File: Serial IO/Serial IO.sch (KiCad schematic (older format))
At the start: 28 parts, among them J1 Apple ][ Peripheral Adapter, J2 BaseboardConnector, J3 SPI Breakout, SW1 Reset Serial, U1 74AHCT04, U2 WD65C21, U3 74LS138, U4 MCP23S17_SP

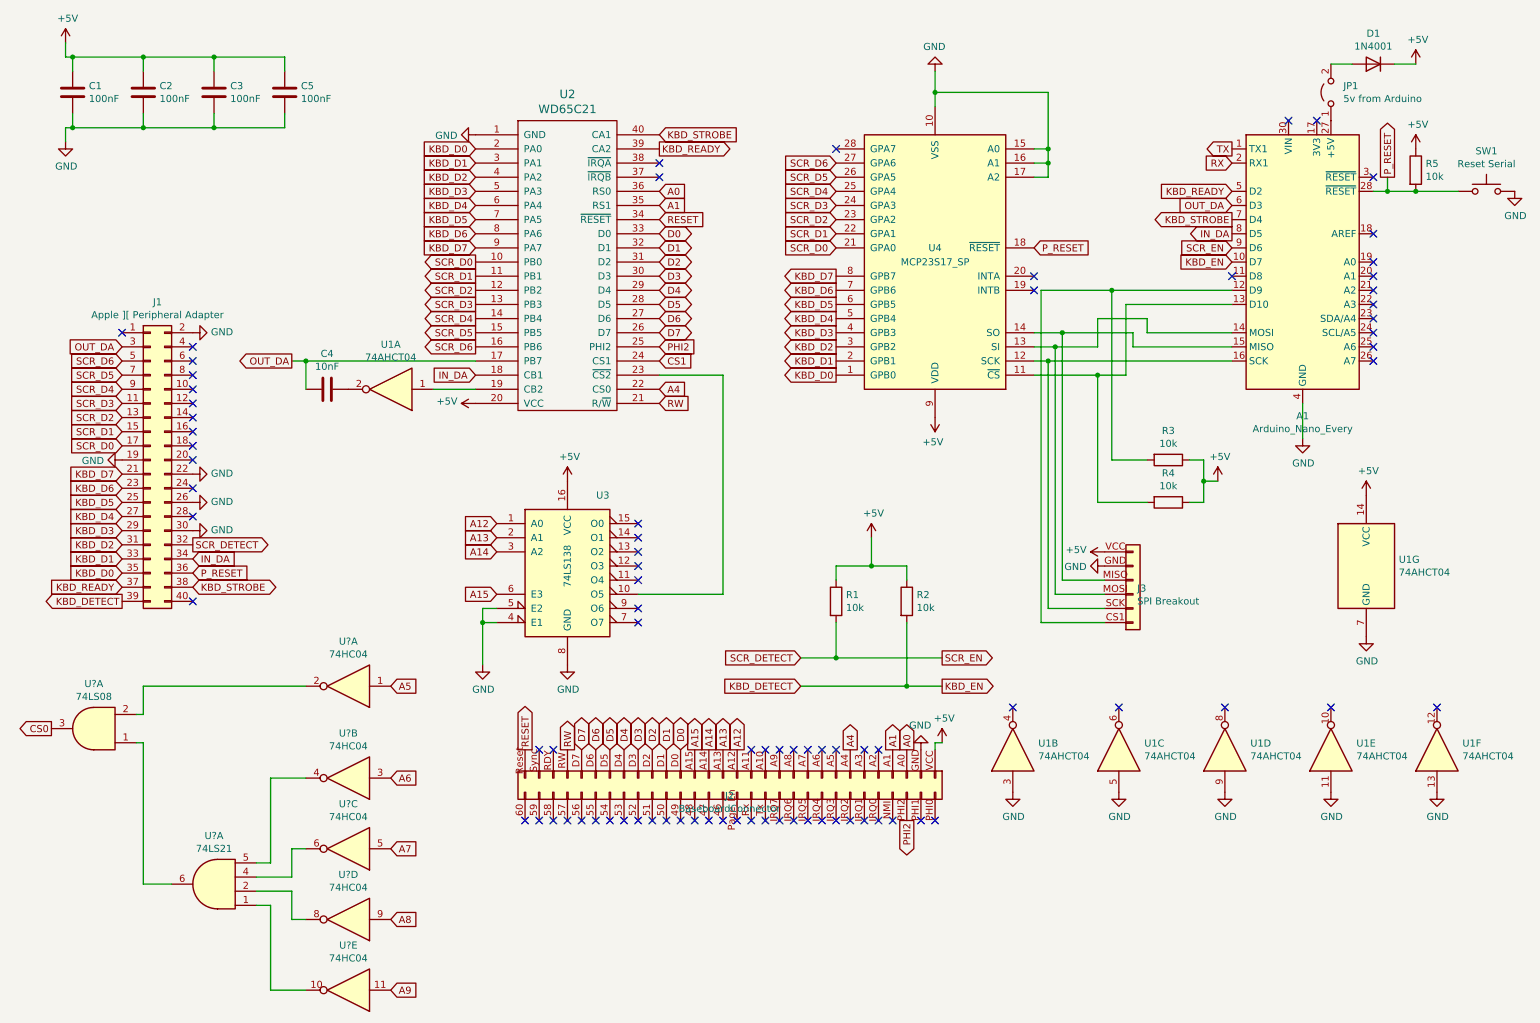
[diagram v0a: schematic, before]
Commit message: Updated Serial IO to use the 6522 VIA instead of the 6521 PIA
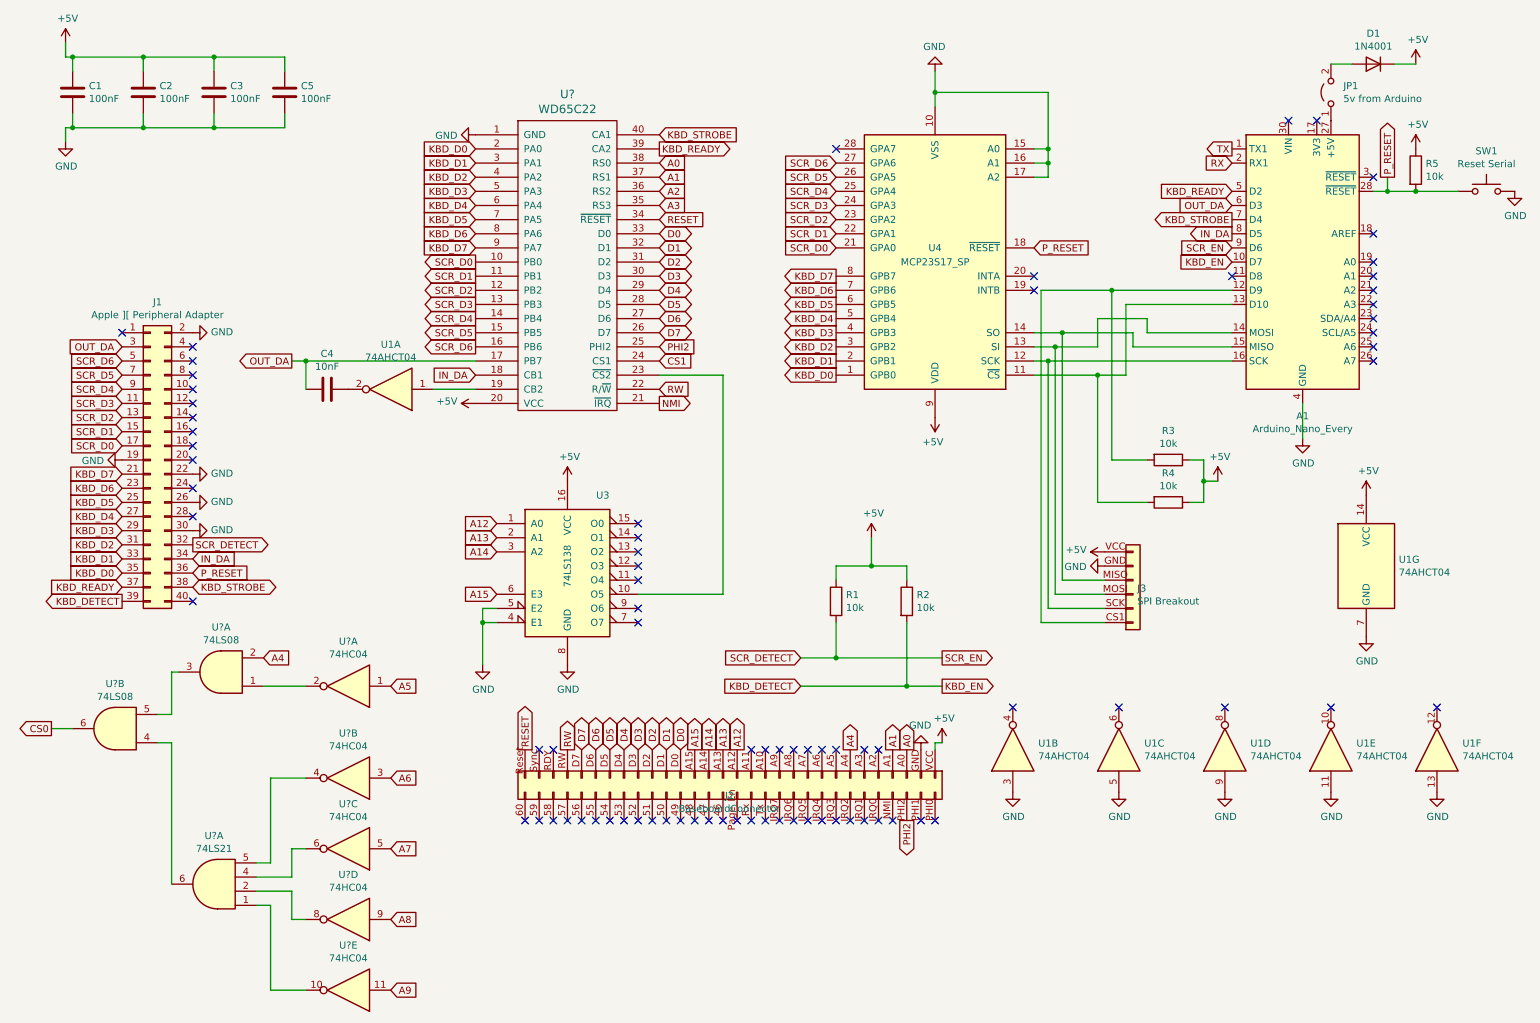
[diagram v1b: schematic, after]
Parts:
- removed U2: WD65C21, Package_DIP:DIP-40_W15.24mm_Socket_LongPads, symbol 65xx:WD65C21
- added U?: WD65C22, symbol 65xx:WD65C22
- added U?: 74LS08, symbol 74xx:74LS08
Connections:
- net +5V: now also U?.20 (VCC)
- net A0: now also U?.38 (RS0)
- net A1: now also U?.37 (RS1)
- net A4: now also U?.2
- net CS0: now also U?.6; no longer U?.3
- net CS1: now also U?.24 (CS1)
- net D0: now also U?.33 (D0)
- net D1: now also U?.32 (D1)
- net D2: now also U?.31 (D2)
- net D3: now also U?.30 (D3)
- net D4: now also U?.29 (D4)
- net D5: now also U?.28 (D5)
- net D6: now also U?.27 (D6)
- net D7: now also U?.26 (D7)
- net GND: now also U?.1 (GND)
- net IN_DA: now also U?.18 (CB1)
- net KBD_D0: now also U?.2 (PA0)
- net KBD_D1: now also U?.3 (PA1)
- net KBD_D2: now also U?.4 (PA2)
- net KBD_D3: now also U?.5 (PA3)
- net KBD_D4: now also U?.6 (PA4)
- net KBD_D5: now also U?.7 (PA5)
- net KBD_D6: now also U?.8 (PA6)
- net KBD_D7: now also U?.9 (PA7)
- net KBD_READY: now also U?.39 (CA2)
- net KBD_STROBE: now also U?.40 (CA1)
- net OUT_DA: now also U?.17 (PB7)
- net PHI2: now also U?.25 (PHI2)
- net RESET: now also U?.34 (~RESET)
- net RW: now also U?.22 (R/~W)
- net SCR_D0: now also U?.10 (PB0)
- net SCR_D1: now also U?.11 (PB1)
- net SCR_D2: now also U?.12 (PB2)
- net SCR_D3: now also U?.13 (PB3)
- net SCR_D4: now also U?.14 (PB4)
- net SCR_D5: now also U?.15 (PB5)
- net SCR_D6: now also U?.16 (PB6)
- net at U1.1: now also U?.19 (CB2)
- net at U3.10 (O5): now also U?.23 (~CS2)
- net at U?.6: now also U?.4; no longer U?.1
- net at U?.2: now also U?.1; no longer U?.2
- new net: U?.3, U?.5
- new net A2: U?.36 (RS2)
- new net A3: U?.35 (RS3)
- new net NMI: U?.21 (~IRQ)
- no-connect marks 83 -> 81
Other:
- moved on the sheet: U?A
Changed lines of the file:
@@
 Text GLabel 6250 2450 0    50   Output ~ 0
 KBD_D7
-NoConn ~ 5000 1650
-NoConn ~ 5000 1750
 Text GLabel 5000 2050 2    50   Input ~ 0
 RESET
-Text GLabel 5000 1850 2    50   Input ~ 0
-A0
-Text GLabel 5000 1950 2    50   Input ~ 0
-A1
 $Comp
 L power:+5V #PWR0110
@@
 PHI2
 Text GLabel 5000 3250 2    50   Input ~ 0
-A4
-Text GLabel 5000 3350 2    50   Input ~ 0
 RW
 Text GLabel 3700 1550 0    50   Input ~ 0
@@
 Text GLabel 3700 3150 0    50   Input ~ 0
 IN_DA
-$Comp
-L 65xx:WD65C21 U2
-U 1 1 60F3CD3E
-P 4350 2350
-F 0 "U2" H 4350 3537 60  0000 C CNN
-F 1 "WD65C21" H 4350 3431 60  0000 C CNN
-F 2 "Package_DIP:DIP-40_W15.24mm_Socket_LongPads" H 3850 2550 60  0001 C CNN
-F 3 "" H 3850 2550 60  0000 C CNN
-	1    4350 2350
-	1    0    0    -1
-$EndComp
 $Comp
 L Device:C C4
@@
 L 74xx:74LS08 U?
 U 1 1 6105548A
-P 1000 5650
-F 0 "U?" H 1000 5333 50  0000 C CNN
-F 1 "74LS08" H 1000 5424 50  0000 C CNN
-F 2 "" H 1000 5650 50  0001 C CNN
-F 3 "http://www.ti.com/lit/gpn/sn74LS08" H 1000 5650 50  0001 C CNN
-	1    1000 5650
+P 1900 5250
+F 0 "U?" H 1900 4933 50  0000 C CNN
+F 1 "74LS08" H 1900 5024 50  0000 C CNN
+F 2 "" H 1900 5250 50  0001 C CNN
+F 3 "http://www.ti.com/lit/gpn/sn74LS08" H 1900 5250 50  0001 C CNN
+	1    1900 5250
 	-1   0    0    1
 $EndComp
@@
 Text GLabel 5000 3050 2    50   Input ~ 0
 CS1
-Wire Wire Line
-	1300 5750 1350 5750
 Wire Wire Line
 	2150 6600 2250 6600
@@
 	-1   0    0    1
 $EndComp
-Wire Wire Line
-	1350 6750 1550 6750
-Wire Wire Line
-	1350 5750 1350 6750
-Wire Wire Line
-	1300 5550 1350 5550
-Wire Wire Line
-	1350 5550 1350 5350
-Wire Wire Line
-	2500 5350 1350 5350
 Text GLabel 3100 5350 2    50   Input ~ 0
 A5
@@
 Text GLabel 3100 7500 2    50   Input ~ 0
 A9
+$Comp
+L 65xx:WD65C22 U?
+U 1 1 610F7212
+P 4350 2350
+F 0 "U?" H 4350 3537 60  0000 C CNN
+F 1 "WD65C22" H 4350 3431 60  0000 C CNN
+F 2 "" H 3850 2550 60  0000 C CNN
+F 3 "" H 3850 2550 60  0000 C CNN
+	1    4350 2350
+	1    0    0    -1
+$EndComp
+Text GLabel 5000 3350 2    50   Output ~ 0
+NMI
+Text GLabel 2200 5150 2    50   Input ~ 0
+A4
+$Comp
+L 74xx:74LS08 U?
+U 2 1 6112490A
+P 1150 5650
+F 0 "U?" H 1150 5333 50  0000 C CNN
+F 1 "74LS08" H 1150 5424 50  0000 C CNN
+F 2 "" H 1150 5650 50  0001 C CNN
+F 3 "http://www.ti.com/lit/gpn/sn74LS08" H 1150 5650 50  0001 C CNN
+	2    1150 5650
+	-1   0    0    1
+$EndComp
+Wire Wire Line
+	700  5650 850  5650
+Wire Wire Line
+	1450 5550 1550 5550
+Wire Wire Line
+	1550 5550 1550 5250
+Wire Wire Line
+	1550 5250 1600 5250
+Wire Wire Line
+	1450 5750 1550 5750
+Wire Wire Line
+	1550 5750 1550 6750
+Wire Wire Line
+	2200 5350 2500 5350
+Text GLabel 5000 1650 2    50   Input ~ 0
+A0
+Text GLabel 5000 1750 2    50   Input ~ 0
+A1
+Text GLabel 5000 1850 2    50   Input ~ 0
+A2
+Text GLabel 5000 1950 2    50   Input ~ 0
+A3
 $EndSCHEMATC

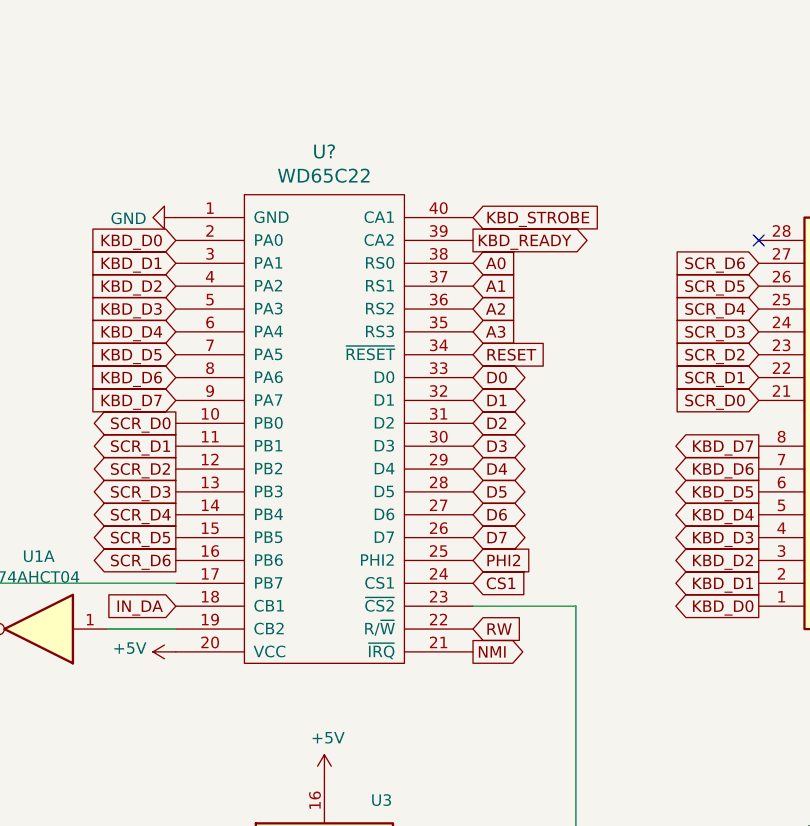
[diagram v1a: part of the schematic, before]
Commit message: Restored SerialIO back to 6521 PIA...
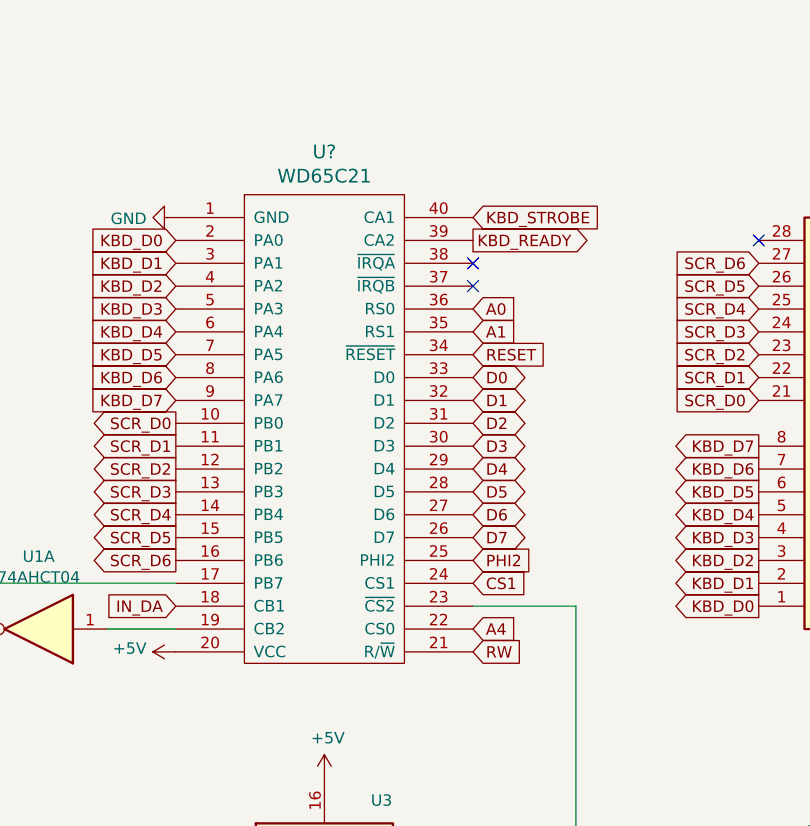
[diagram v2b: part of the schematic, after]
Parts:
- removed U?: WD65C22, symbol 65xx:WD65C22
- added U?: WD65C21, symbol 65xx:WD65C21
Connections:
- net +5V: now also U?.20 (VCC)
- net A0: now also U?.36 (RS0)
- net A1: now also U?.35 (RS1)
- net A4: now also U?.22 (CS0)
- net CS1: now also U?.24 (CS1)
- net D0: now also U?.33 (D0)
- net D1: now also U?.32 (D1)
- net D2: now also U?.31 (D2)
- net D3: now also U?.30 (D3)
- net D4: now also U?.29 (D4)
- net D5: now also U?.28 (D5)
- net D6: now also U?.27 (D6)
- net D7: now also U?.26 (D7)
- net GND: now also U?.1 (GND)
- net IN_DA: now also U?.18 (CB1)
- net KBD_D0: now also U?.2 (PA0)
- net KBD_D1: now also U?.3 (PA1)
- net KBD_D2: now also U?.4 (PA2)
- net KBD_D3: now also U?.5 (PA3)
- net KBD_D4: now also U?.6 (PA4)
- net KBD_D5: now also U?.7 (PA5)
- net KBD_D6: now also U?.8 (PA6)
- net KBD_D7: now also U?.9 (PA7)
- net KBD_READY: now also U?.39 (CA2)
- net KBD_STROBE: now also U?.40 (CA1)
- net OUT_DA: now also U?.17 (PB7)
- net PHI2: now also U?.25 (PHI2)
- net RESET: now also U?.34 (~RESET)
- net RW: now also U?.21 (R/~W)
- net SCR_D0: now also U?.10 (PB0)
- net SCR_D1: now also U?.11 (PB1)
- net SCR_D2: now also U?.12 (PB2)
- net SCR_D3: now also U?.13 (PB3)
- net SCR_D4: now also U?.14 (PB4)
- net SCR_D5: now also U?.15 (PB5)
- net SCR_D6: now also U?.16 (PB6)
- net at U3.10 (O5): now also U?.23 (~CS2)
- net at U1.1: now also U?.19 (CB2)
- no-connect marks 81 -> 83
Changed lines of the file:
@@
 Text GLabel 5000 2950 2    50   Input ~ 0
 PHI2
-Text GLabel 5000 3250 2    50   Input ~ 0
-RW
 Text GLabel 3700 1550 0    50   Input ~ 0
 KBD_D0
@@
 Text GLabel 3100 7500 2    50   Input ~ 0
 A9
-$Comp
-L 65xx:WD65C22 U?
-U 1 1 610F7212
-P 4350 2350
-F 0 "U?" H 4350 3537 60  0000 C CNN
-F 1 "WD65C22" H 4350 3431 60  0000 C CNN
-F 2 "" H 3850 2550 60  0000 C CNN
-F 3 "" H 3850 2550 60  0000 C CNN
-	1    4350 2350
-	1    0    0    -1
-$EndComp
-Text GLabel 5000 3350 2    50   Output ~ 0
-NMI
 Text GLabel 2200 5150 2    50   Input ~ 0
 A4
@@
 Wire Wire Line
 	2200 5350 2500 5350
-Text GLabel 5000 1650 2    50   Input ~ 0
+$Comp
+L 65xx:WD65C21 U?
+U 1 1 61115C53
+P 4350 2350
+F 0 "U?" H 4350 3537 60  0000 C CNN
+F 1 "WD65C21" H 4350 3431 60  0000 C CNN
+F 2 "" H 3850 2550 60  0000 C CNN
+F 3 "" H 3850 2550 60  0000 C CNN
+	1    4350 2350
+	1    0    0    -1
+$EndComp
+NoConn ~ 5000 1650
+NoConn ~ 5000 1750
+Text GLabel 5000 1850 2    50   Input ~ 0
 A0
-Text GLabel 5000 1750 2    50   Input ~ 0
+Text GLabel 5000 1950 2    50   Input ~ 0
 A1
-Text GLabel 5000 1850 2    50   Input ~ 0
-A2
-Text GLabel 5000 1950 2    50   Input ~ 0
-A3
+Text GLabel 5000 3250 2    50   Input ~ 0
+A4
+Text GLabel 5000 3350 2    50   Input ~ 0
+RW
 $EndSCHEMATC
